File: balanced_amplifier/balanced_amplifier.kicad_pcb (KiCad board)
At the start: 2 copper layers, 117 parts, among them J1 Conn_01x04_Male, J2 Conn_01x04_Male, J3 Screw_Terminal_01x03, J4 Conn_01x04_Male, J5 Conn_01x04_Male, U1 LM4562, U2 LM4562, U3 NE5532, U4 LM4562, U5 LM4562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

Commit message: consolidate components in center of page
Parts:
- moved C100 138.2 mm to (59.7, 175.3)
- moved C101 138.2 mm to (67.3, 175.3)
- moved J3 138.2 mm to (61.0, 186.7)
- moved C15 105.2 mm to (118.1, 130.8)
- moved C18 105.2 mm to (111.8, 123.2)
- moved C5 105.2 mm to (109.2, 110.5)
- moved C6 105.2 mm to (102.9, 110.5)
- moved C7 105.2 mm to (118.1, 119.4)
- moved R11 105.2 mm to (103.7, 105.4)
- moved R21 105.2 mm to (102.7, 132.1)
- moved R24 105.2 mm to (95.2, 132.1)
- moved R8 105.2 mm to (108.8, 105.4)
- moved TP3 105.2 mm to (116.8, 102.9)
- moved TP6 105.2 mm to (121.9, 144.8)
- moved U2 105.2 mm to (102.9, 123.2)
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
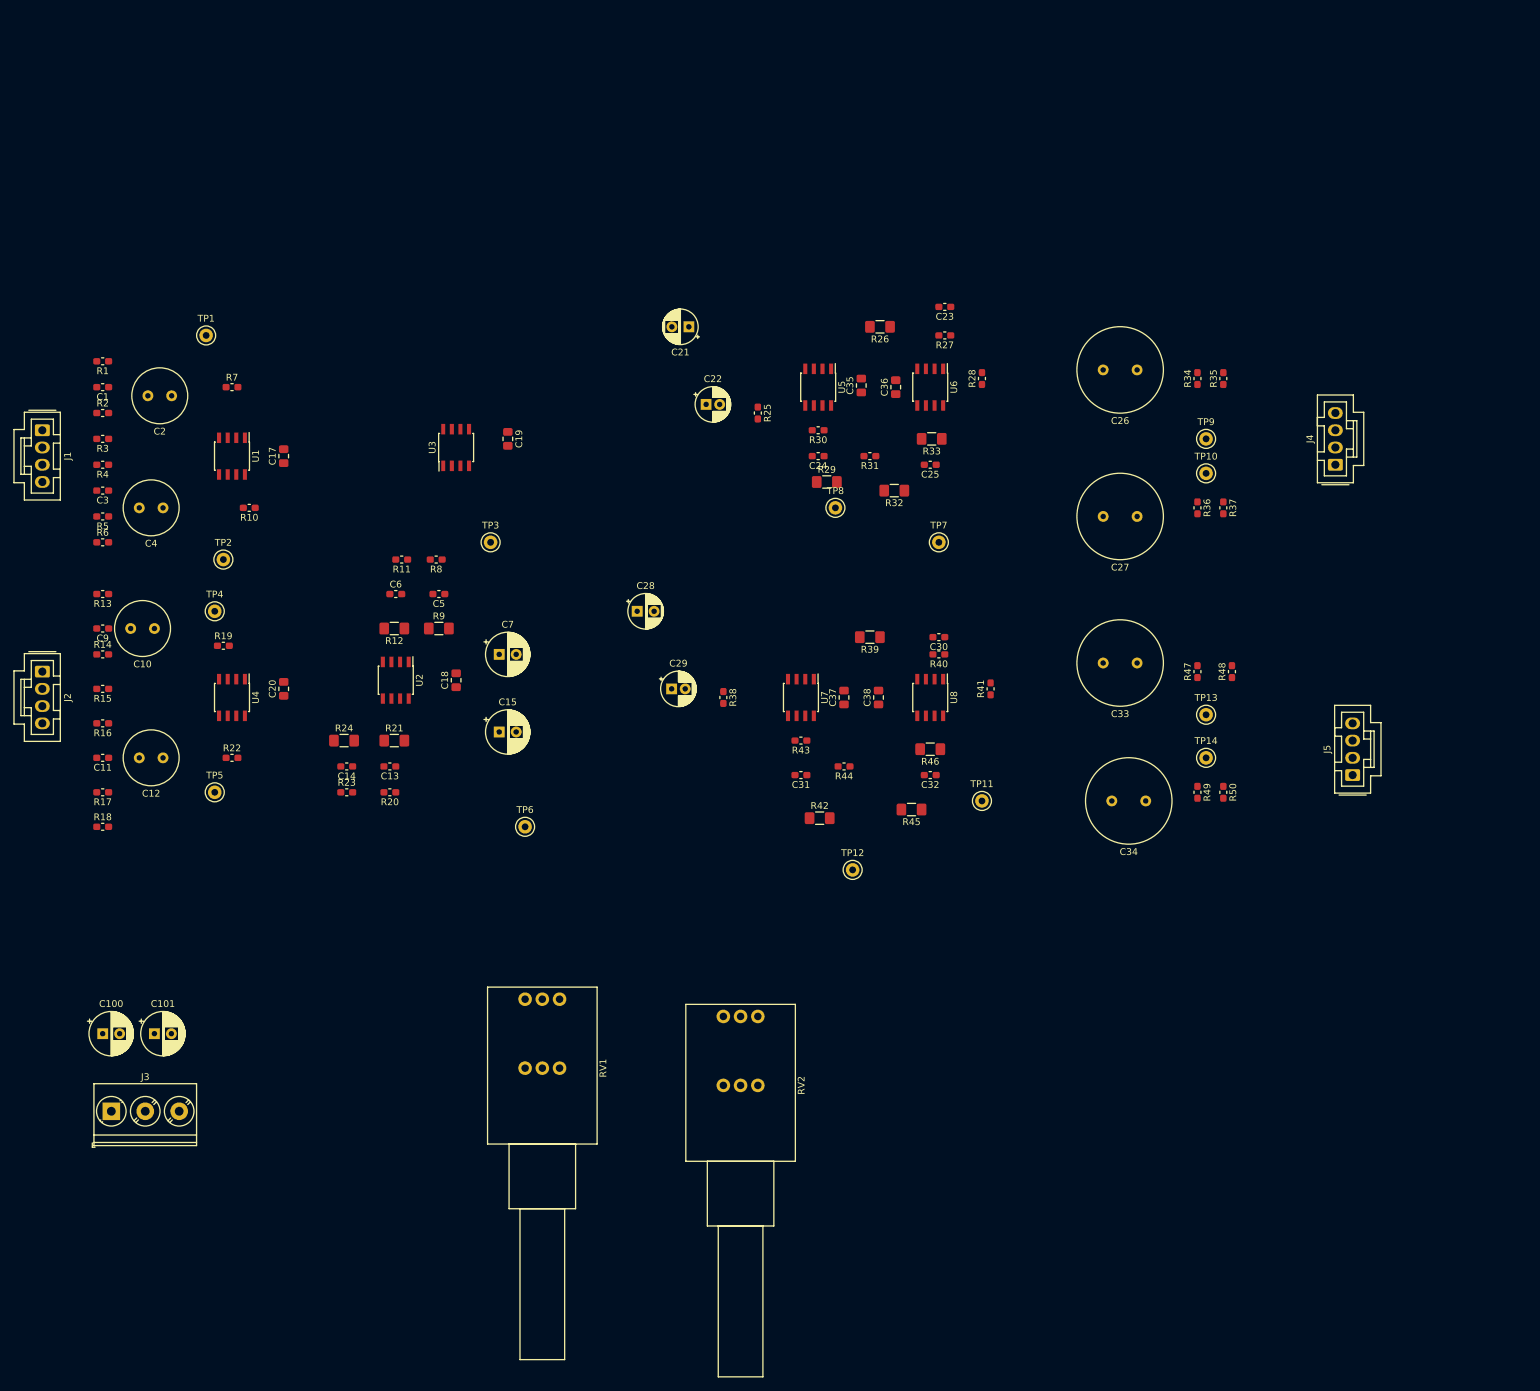
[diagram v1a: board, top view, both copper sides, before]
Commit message: Initial layout of input amplifier (incomplete)
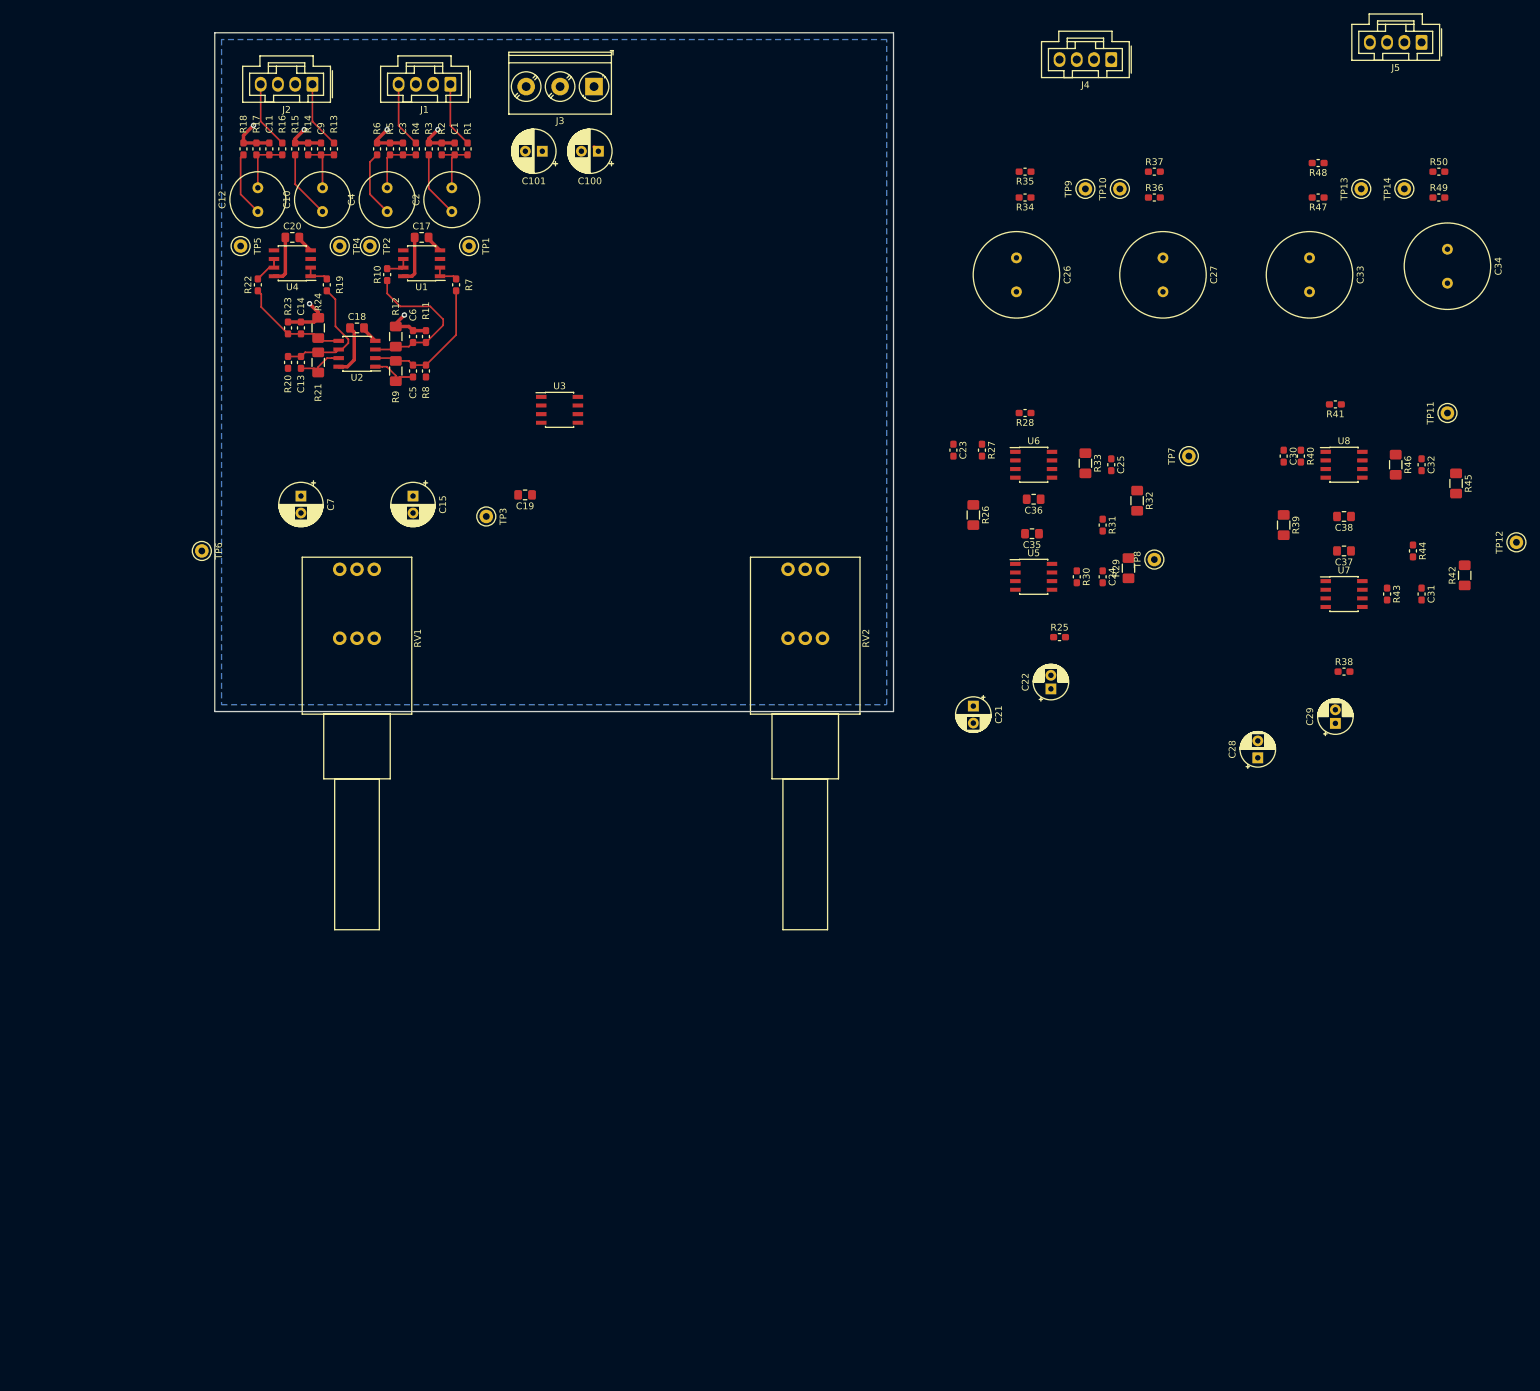
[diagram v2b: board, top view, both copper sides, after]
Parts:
- moved J3 166.9 mm to (132.1, 35.7), turned to 180 degrees
- moved C100 149.1 mm to (132.7, 45.2), turned to 180 degrees
- moved C101 142.0 mm to (124.5, 45.2), turned to 180 degrees
- moved TP12 109.1 mm to (268.0, 102.9), turned to 90 degrees
- moved J5 108.4 mm to (254.0, 29.2), turned to 180 degrees
- moved R18 102.0 mm to (80.4, 44.9), turned to 270 degrees
- moved R42 101.5 mm to (260.4, 107.7), turned to 90 degrees
- moved C29 97.9 mm to (241.3, 129.5), turned to 90 degrees
- moved R17 97.5 mm to (82.3, 44.9), turned to 90 degrees
- moved R50 96.8 mm to (256.5, 48.3), turned to 0 degrees
- moved C31 95.2 mm to (254.0, 110.5), turned to 270 degrees
- moved J2 95.2 mm to (90.6, 35.4), turned to 180 degrees
- moved R49 94.6 mm to (256.5, 52.1), turned to 0 degrees
- moved C28 94.0 mm to (229.9, 134.6), turned to 90 degrees
- moved R45 93.5 mm to (259.1, 94.2), turned to 270 degrees
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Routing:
- net GNDA: track 0.00 -> 40.3 mm, vias 0 -> 6
- net Net-(C6-Pad1): track 0.00 -> 24.1 mm
- net VCC: track 0.00 -> 22.9 mm
- net Net-(C5-Pad2): track 0.00 -> 20.7 mm
- net Net-(C13-Pad2): track 0.00 -> 18.7 mm
- net Net-(C14-Pad1): track 0.00 -> 16.1 mm
- net Net-(C10-Pad1): track 0.00 -> 10.5 mm
- net Net-(C2-Pad1): track 0.00 -> 10.2 mm
- net /left_in_hot: track 0.00 -> 9.97 mm
- net /left_in_cold: track 0.00 -> 9.97 mm
- net Net-(C4-Pad1): track 0.00 -> 9.84 mm
- net /right_in_hot: track 0.00 -> 9.70 mm
- net /right_in_cold: track 0.00 -> 9.70 mm
- net Net-(C12-Pad1): track 0.00 -> 9.58 mm
- net Net-(C3-Pad1): track 0.00 -> 8.84 mm
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- added copper zone on B.Cu, net GNDA
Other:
- board outline added: 100 x 100 mm
- net class power/ground added: clearance 0.2, trace_width 0.508, via_dia 0.8, via_drill 0.4

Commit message: complete initial layout of input section
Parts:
- moved U3 30.0 mm to (97.2, 85.9), turned to 180 degrees
- moved C19 28.4 mm to (97.2, 82.1), turned to 0 degrees
- moved TP6 26.3 mm to (89.5, 82.7), turned to 180 degrees
- moved TP3 19.2 mm to (103.5, 84.6), turned to 180 degrees
- moved TP4 18.1 mm to (83.2, 73.2), turned to 180 degrees
- moved TP1 18.0 mm to (111.1, 77.0), turned to 180 degrees
- moved C7 14.7 mm to (103.5, 97.3)
- moved TP2 14.4 mm to (109.9, 68.7), turned to 180 degrees
- moved C15 12.1 mm to (93.3, 97.3)
- moved C100 10.8 mm to (121.9, 44.6)
- moved TP5 8.28 mm to (79.4, 67.5), turned to 180 degrees
- moved C101 7.01 mm to (131.4, 44.6)
- moved R19 1.27 mm to (92.7, 63.7)
- moved R10 0.39 mm to (101.6, 63.0)
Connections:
- J3 pad 1: VCC -> VEE
- J3 pad 3: VEE -> VCC
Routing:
- net Net-(RV1-Pad2): track 0.00 -> 45.1 mm
- net Net-(RV1-Pad5): track 0.00 -> 33.4 mm
- net /volume_control/left_in: track 7.16 -> 30.8 mm
- net Net-(R20-Pad1): track 0.00 -> 22.0 mm
- net Net-(C7-Pad2): track 0.00 -> 20.9 mm
- net /volume_control/right_in: track 7.16 -> 26.5 mm
- net Net-(R8-Pad1): track 0.00 -> 16.9 mm
- net VEE: track 7.97 -> 21.9 mm
- net VCC: track 22.9 -> 33.9 mm
- net Net-(C15-Pad2): track 0.00 -> 9.66 mm
- net Net-(C10-Pad1): track 10.5 -> 18.9 mm, vias 0 -> 1
- net Net-(C2-Pad1): track 10.2 -> 18.1 mm, vias 0 -> 1
- net Net-(C4-Pad1): track 9.84 -> 17.6 mm, vias 0 -> 1
- net Net-(C13-Pad2): track 18.7 -> 25.8 mm, vias 0 -> 1
- net Net-(C12-Pad1): track 9.58 -> 16.3 mm
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- added copper zone on F.Cu, net VCC
- added copper zone on F.Cu, net VEE

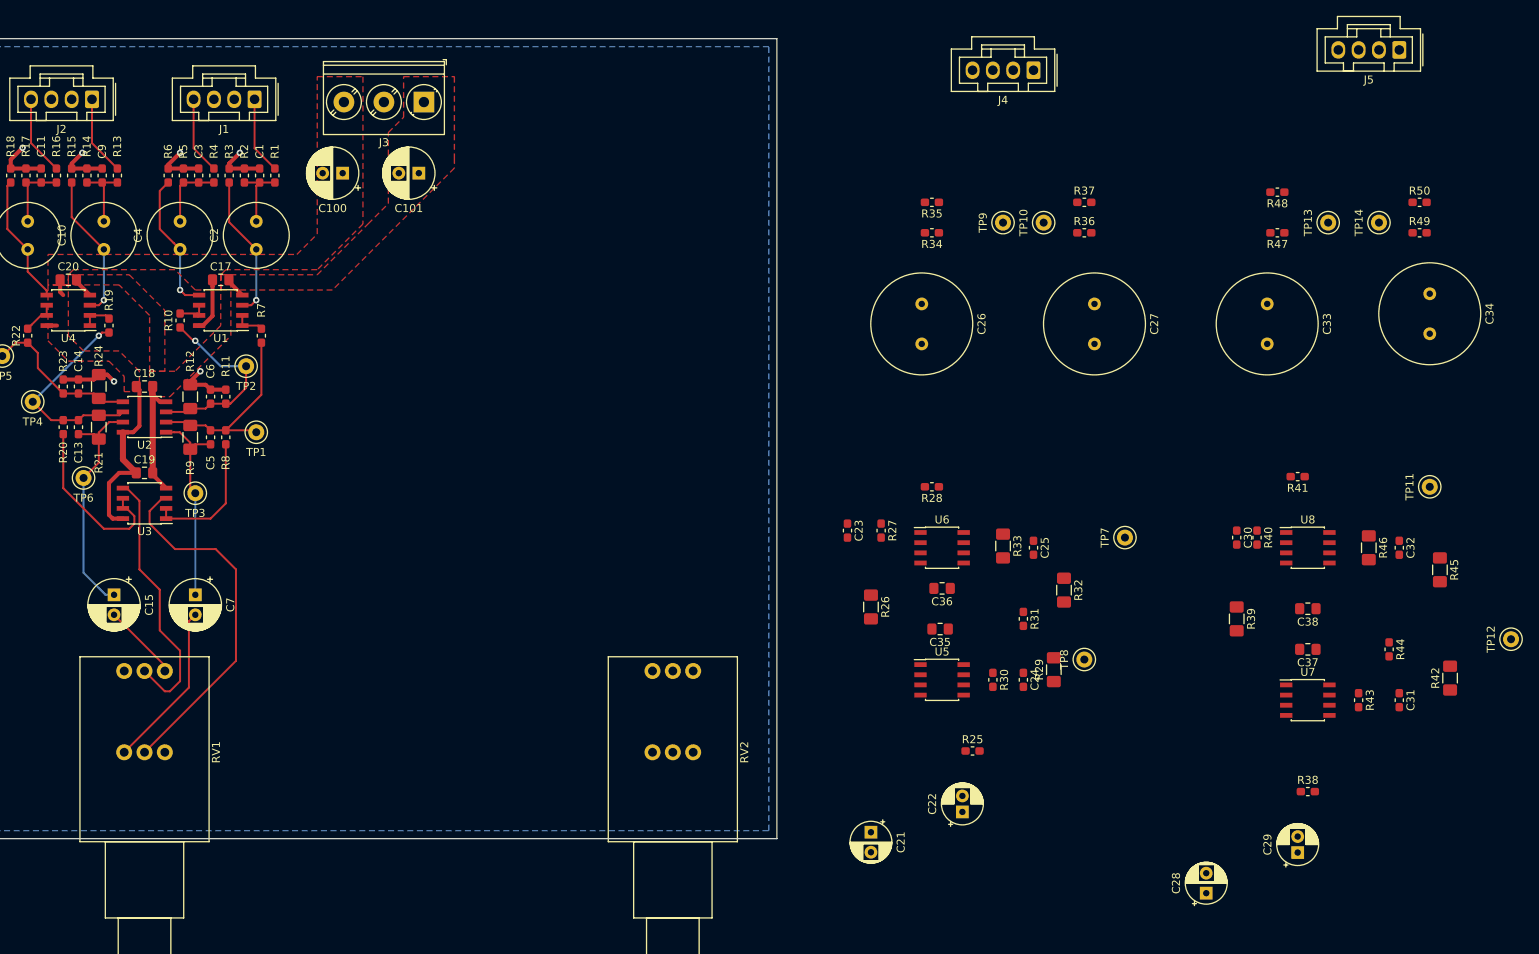
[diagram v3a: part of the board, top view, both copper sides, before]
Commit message: initial placement of volume control circuits
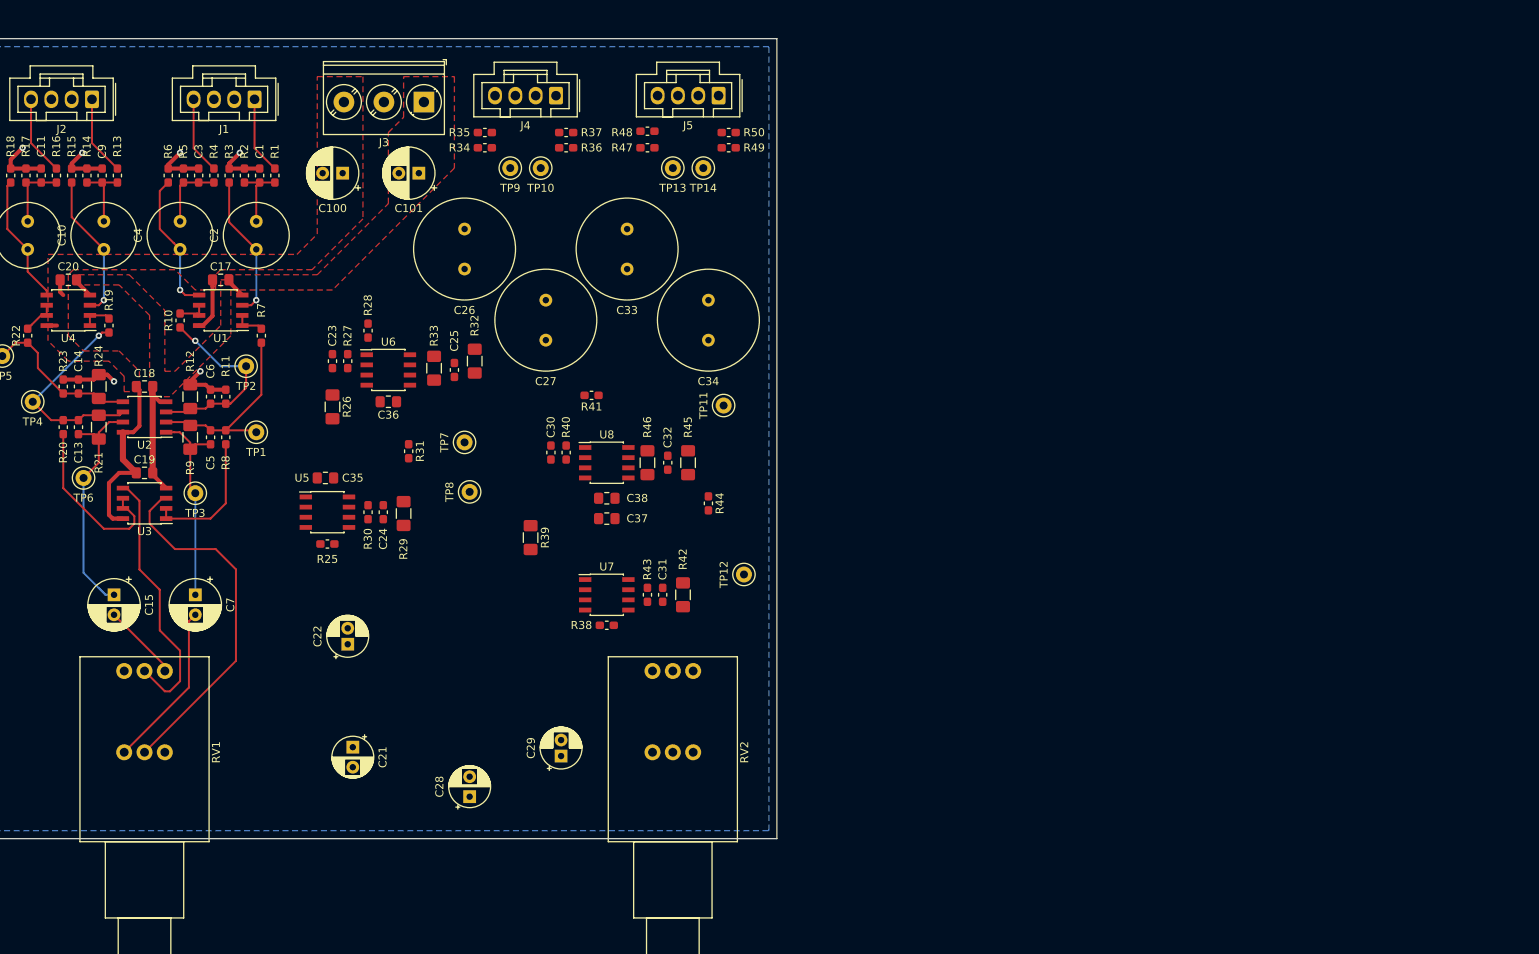
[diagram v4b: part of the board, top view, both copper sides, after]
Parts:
- moved R42 96.4 mm to (164.5, 97.3)
- moved TP12 96.2 mm to (172.1, 94.8)
- moved R45 94.9 mm to (165.1, 80.8), turned to 90 degrees
- moved C31 93.0 mm to (161.9, 97.3)
- moved C28 92.9 mm to (137.8, 122.6)
- moved C29 92.9 mm to (149.2, 117.5)
- moved C32 92.1 mm to (162.6, 80.8)
- moved R46 90.8 mm to (160.0, 80.8)
- moved C34 90.2 mm to (167.6, 60.5)
- moved R38 90.1 mm to (154.9, 101.1)
- moved R43 89.9 mm to (160.0, 97.3)
- moved C37 89.1 mm to (154.9, 87.8)
- moved R39 88.8 mm to (145.4, 90.2)
- moved R41 88.8 mm to (153.0, 72.4)
- moved TP11 88.8 mm to (169.5, 73.7)
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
